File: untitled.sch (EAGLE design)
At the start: 197 parts, among them Q1 CSM-7X-DU, X1 USBC

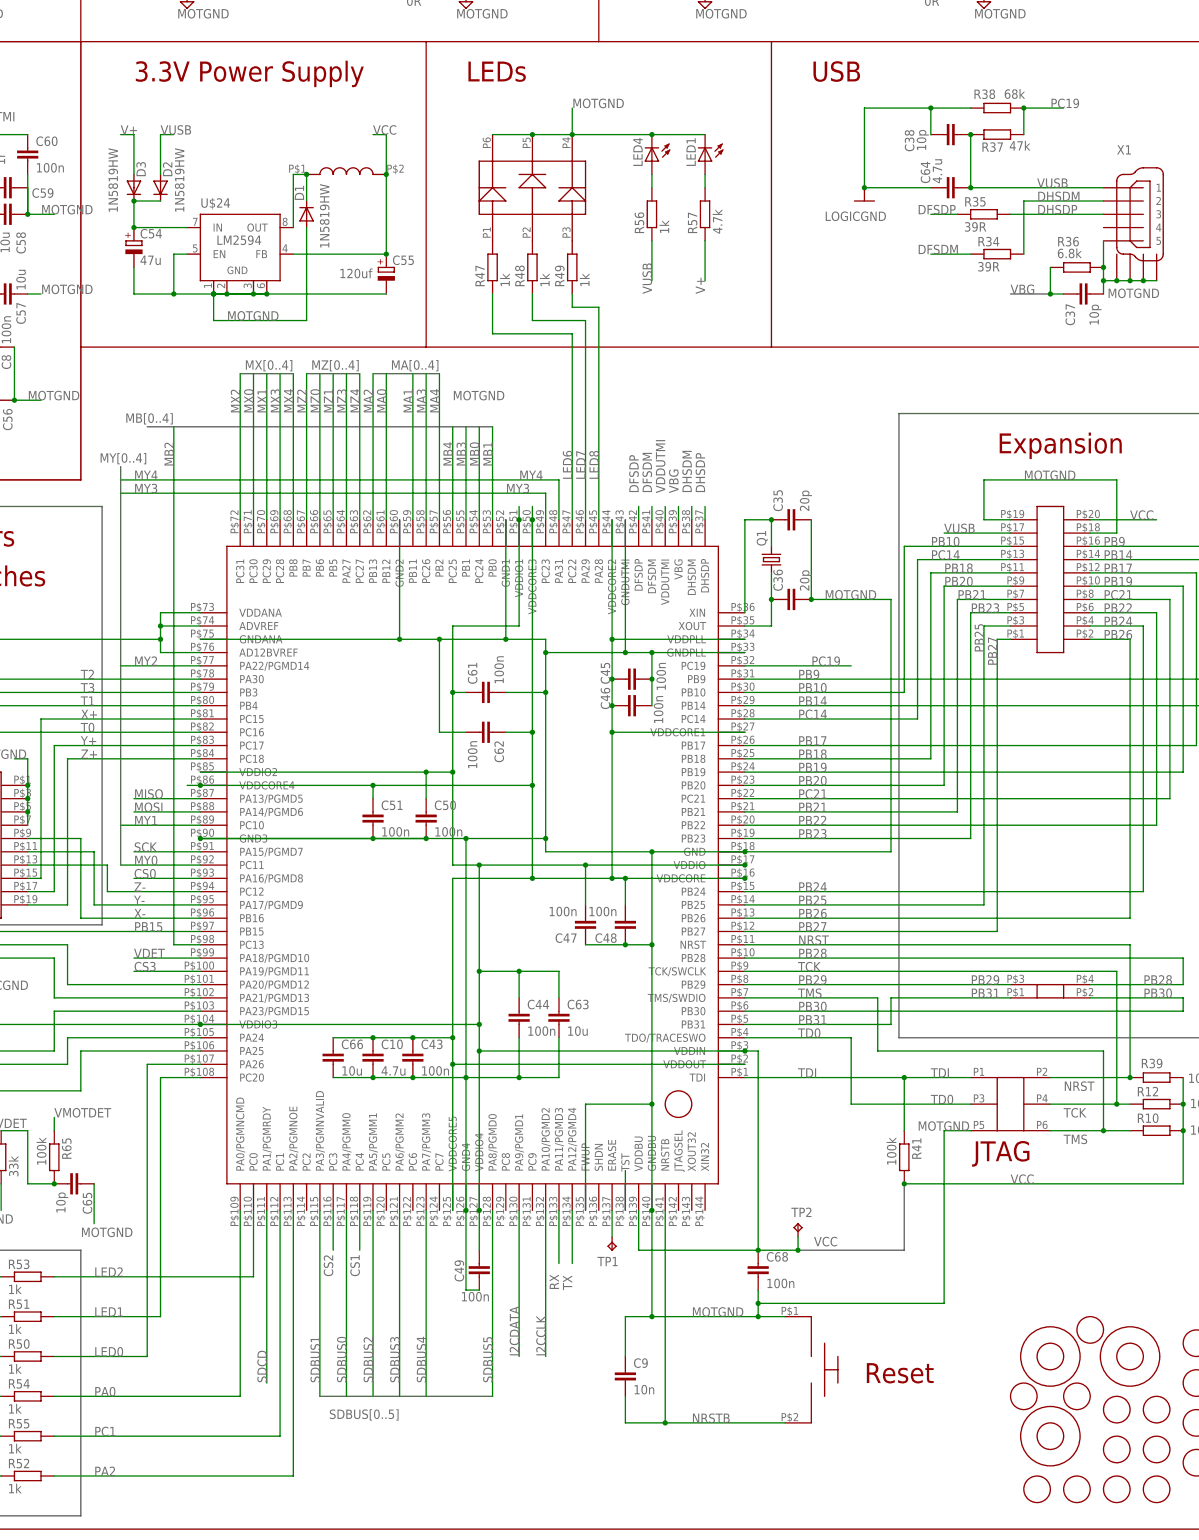
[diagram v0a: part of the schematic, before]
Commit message: Changed LED signal names to match pinmap.txt
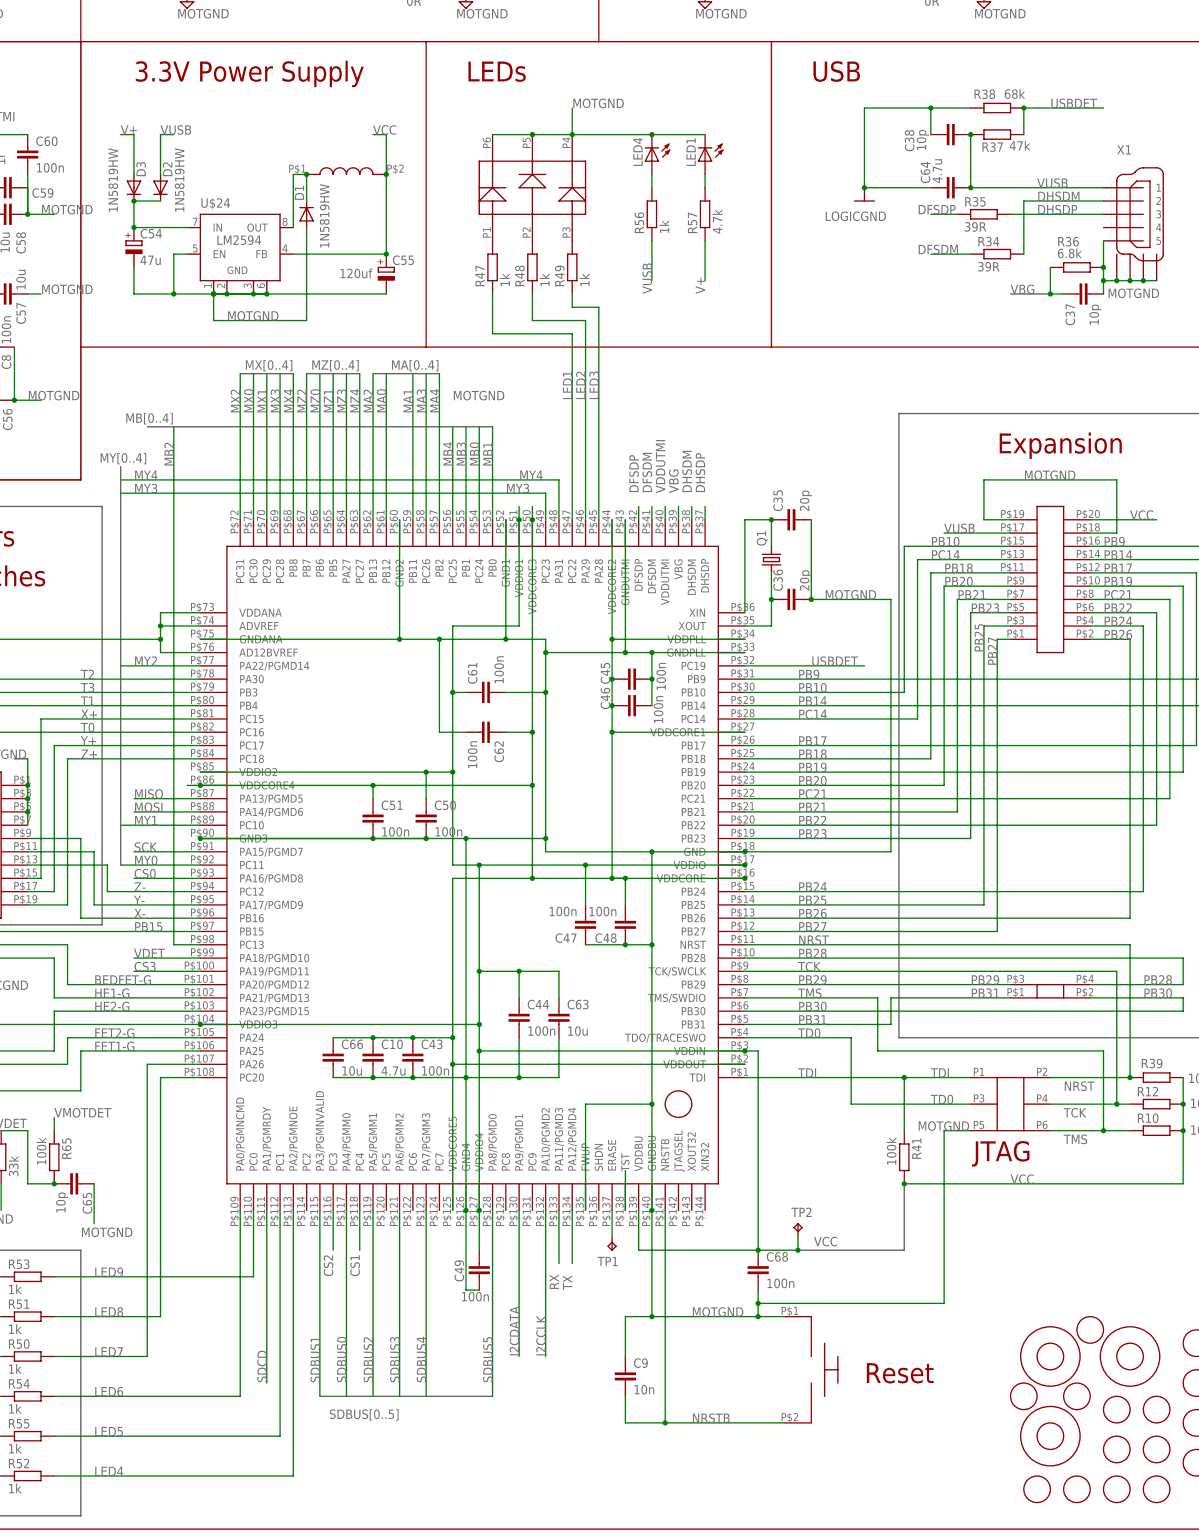
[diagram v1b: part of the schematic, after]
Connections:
- net N$2 renamed HE2-G
- net N$3 renamed HE1-G
- net N$4 renamed BEDFET-G
- net N$8 renamed FET1-G
- net N$88 renamed FET2-G
- net PA2 renamed LED4
- net PC1 renamed LED5
- net PC19 renamed USBDET
- removed net LED0: R50.2, U$8.PA26
- removed net PA0: R54.2, U$8.PA0/PGMNCMD
- new net LED3: R49.1, U$8.PA28
- new net LED9: R53.2, U$8.PC0
- net LED1: now also R47.1, U$8.PC22; no longer R51.2, U$8.PC20
- net LED2: now also R48.1, U$8.PA29; no longer R53.2, U$8.PC0
- net LED6: now also R54.2, U$8.PA0/PGMNCMD; no longer R47.1, U$8.PC22
- net LED7: now also R50.2, U$8.PA26; no longer R48.1, U$8.PA29
- net LED8: now also R51.2, U$8.PC20; no longer R49.1, U$8.PA28
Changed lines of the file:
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@@
 </busses>
 <nets>
-<net name="N$2" class="0">
+<net name="HE2-G" class="0">
 <segment>
 <wire x1="30.48" y1="-58.42" x2="60.96" y2="-58.42" width="0.1524" layer="91"/>
@@
 <pinref part="U$8" gate="G$1" pin="PA23/PGMD15"/>
 <pinref part="R61" gate="G$1" pin="2"/>
+<label x="68.58" y="-50.8" size="1.778" layer="95"/>
 </segment>
 </net>
-<net name="N$3" class="0">
+<net name="HE1-G" class="0">
 <segment>
 <wire x1="60.96" y1="-48.26" x2="88.9" y2="-48.26" width="0.1524" layer="91"/>
@@
 <pinref part="U$8" gate="G$1" pin="PA21/PGMD13"/>
 <pinref part="R62" gate="G$1" pin="2"/>
+<label x="68.58" y="-48.26" size="1.778" layer="95"/>
 </segment>
 </net>
-<net name="N$4" class="0">
+<net name="BEDFET-G" class="0">
 <segment>
 <wire x1="63.5" y1="-45.72" x2="88.9" y2="-45.72" width="0.1524" layer="91"/>
@@
 <pinref part="U$8" gate="G$1" pin="PA20/PGMD12"/>
 <pinref part="R58" gate="G$1" pin="2"/>
+<label x="68.58" y="-45.72" size="1.778" layer="95"/>
 </segment>
 </net>
@@
 </segment>
 </net>
-<net name="N$8" class="0">
+<net name="FET1-G" class="0">
 <segment>
 <wire x1="66.04" y1="-66.04" x2="66.04" y2="-58.42" width="0.1524" layer="91"/>
@@
 <pinref part="U$8" gate="G$1" pin="PA25"/>
 <pinref part="R60" gate="G$1" pin="2"/>
+<label x="68.58" y="-58.42" size="1.778" layer="95"/>
 </segment>
 </net>
@@
 </segment>
 </net>
-<net name="N$88" class="0">
+<net name="FET2-G" class="0">
 <segment>
 <wire x1="17.78" y1="-78.74" x2="25.4" y2="-78.74" width="0.1524" layer="91"/>
@@
 <pinref part="U$8" gate="G$1" pin="PA24"/>
 <pinref part="R59" gate="G$1" pin="1"/>
+<label x="68.58" y="-55.88" size="1.778" layer="95"/>
 </segment>
 </net>
@@
 </segment>
 </net>
-<net name="LED8" class="0">
+<net name="LED3" class="0">
 <segment>
 <wire x1="165.1" y1="43.18" x2="165.1" y2="83.82" width="0.1524" layer="91"/>
@@
 <pinref part="U$8" gate="G$1" pin="PA28"/>
 <pinref part="R49" gate="G$1" pin="1"/>
-<label x="165.1" y="50.8" size="1.778" layer="95" rot="R90"/>
+<label x="165.1" y="66.04" size="1.778" layer="95" rot="R90"/>
 </segment>
 </net>
-<net name="LED7" class="0">
+<net name="LED2" class="0">
 <segment>
 <wire x1="162.56" y1="43.18" x2="162.56" y2="81.28" width="0.1524" layer="91"/>
@@
 <pinref part="U$8" gate="G$1" pin="PA29"/>
 <pinref part="R48" gate="G$1" pin="1"/>
-<label x="162.56" y="50.8" size="1.778" layer="95" rot="R90"/>
+<label x="162.56" y="66.04" size="1.778" layer="95" rot="R90"/>
 </segment>
 </net>
-<net name="LED6" class="0">
+<net name="LED1" class="0">
 <segment>
 <wire x1="160.02" y1="43.18" x2="160.02" y2="78.74" width="0.1524" layer="91"/>
@@
 <pinref part="U$8" gate="G$1" pin="PC22"/>
 <pinref part="R47" gate="G$1" pin="1"/>
-<label x="160.02" y="50.8" size="1.778" layer="95" rot="R90"/>
+<label x="160.02" y="66.04" size="1.778" layer="95" rot="R90"/>
 </segment>
 </net>
-<net name="LED0" class="0">
+<net name="LED7" class="0">
 <segment>
 <wire x1="60.96" y1="-116.84" x2="78.74" y2="-116.84" width="0.1524" layer="91"/>
@@
 </segment>
 </net>
-<net name="LED1" class="0">
+<net name="LED8" class="0">
 <segment>
 <wire x1="88.9" y1="-63.5" x2="81.28" y2="-63.5" width="0.1524" layer="91"/>
@@
 </segment>
 </net>
-<net name="LED2" class="0">
+<net name="LED9" class="0">
 <segment>
 <wire x1="60.96" y1="-101.6" x2="99.06" y2="-101.6" width="0.1524" layer="91"/>
@@
 </segment>
 </net>
-<net name="PA0" class="0">
+<net name="LED6" class="0">
 <segment>
 <wire x1="60.96" y1="-124.46" x2="96.52" y2="-124.46" width="0.1524" layer="91"/>
@@
 </segment>
 </net>
-<net name="PC1" class="0">
+<net name="LED5" class="0">
 <segment>
 <wire x1="60.96" y1="-132.08" x2="104.14" y2="-132.08" width="0.1524" layer="91"/>
@@
 </segment>
 </net>
-<net name="PA2" class="0">
+<net name="LED4" class="0">
 <segment>
 <wire x1="60.96" y1="-139.7" x2="106.68" y2="-139.7" width="0.1524" layer="91"/>
@@
 </segment>
 </net>
-<net name="PC19" class="0">
+<net name="USBDET" class="0">
 <segment>
-<wire x1="246.38" y1="121.92" x2="254" y2="121.92" width="0.1524" layer="91"/>
+<wire x1="215.9" y1="15.24" x2="193.04" y2="15.24" width="0.1524" layer="91"/>
+<pinref part="U$8" gate="G$1" pin="PC19"/>
+<label x="205.74" y="15.24" size="1.778" layer="95"/>
+</segment>
+<segment>
+<pinref part="R37" gate="G$1" pin="1"/>
 <junction x="246.38" y="121.92"/>
 <pinref part="R38" gate="G$1" pin="2"/>
-<pinref part="R37" gate="G$1" pin="1"/>
+<wire x1="261.62" y1="121.92" x2="246.38" y2="121.92" width="0.1524" layer="91"/>
 <wire x1="246.38" y1="121.92" x2="246.38" y2="116.84" width="0.1524" layer="91"/>
 <label x="251.46" y="121.92" size="1.778" layer="95"/>
 </segment>
-<segment>
-<wire x1="213.36" y1="15.24" x2="193.04" y2="15.24" width="0.1524" layer="91"/>
-<pinref part="U$8" gate="G$1" pin="PC19"/>
-<label x="205.74" y="15.24" size="1.778" layer="95"/>
-</segment>
 </net>
